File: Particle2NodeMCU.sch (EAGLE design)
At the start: 6 parts

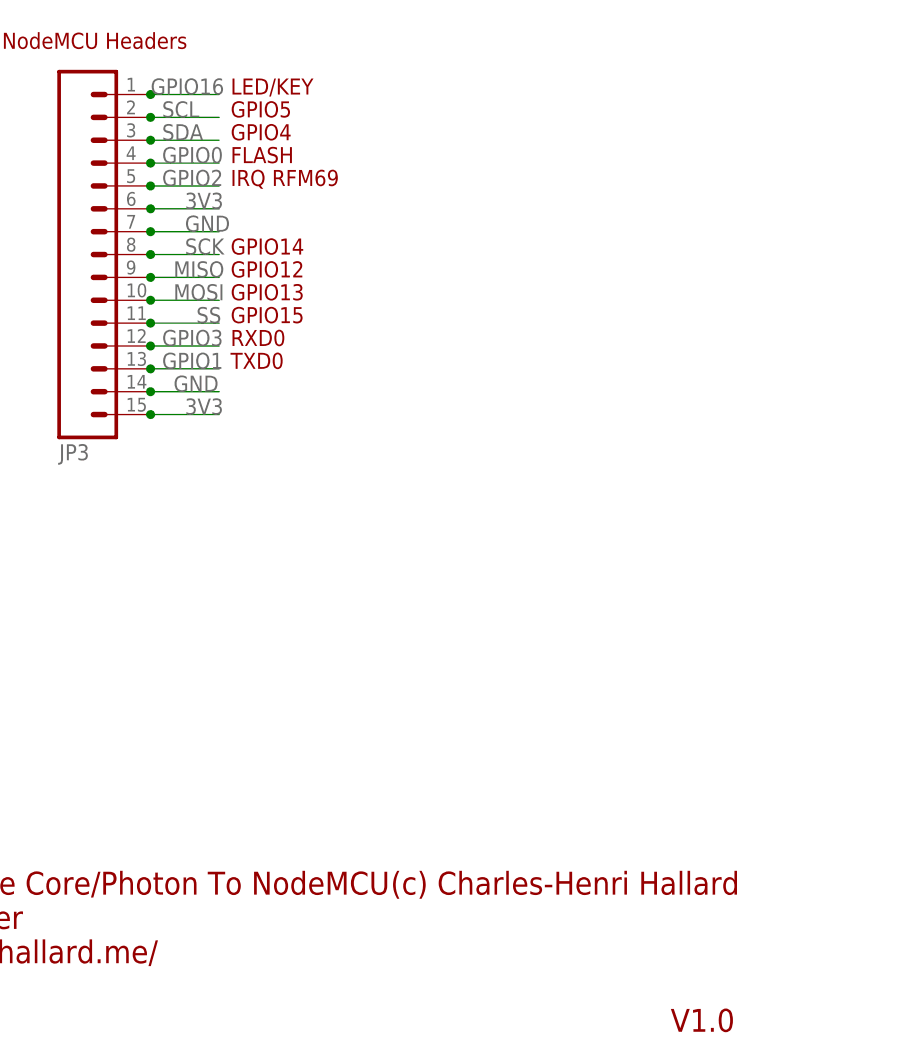
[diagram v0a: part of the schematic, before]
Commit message: Fixed GPIO now version 1.0a
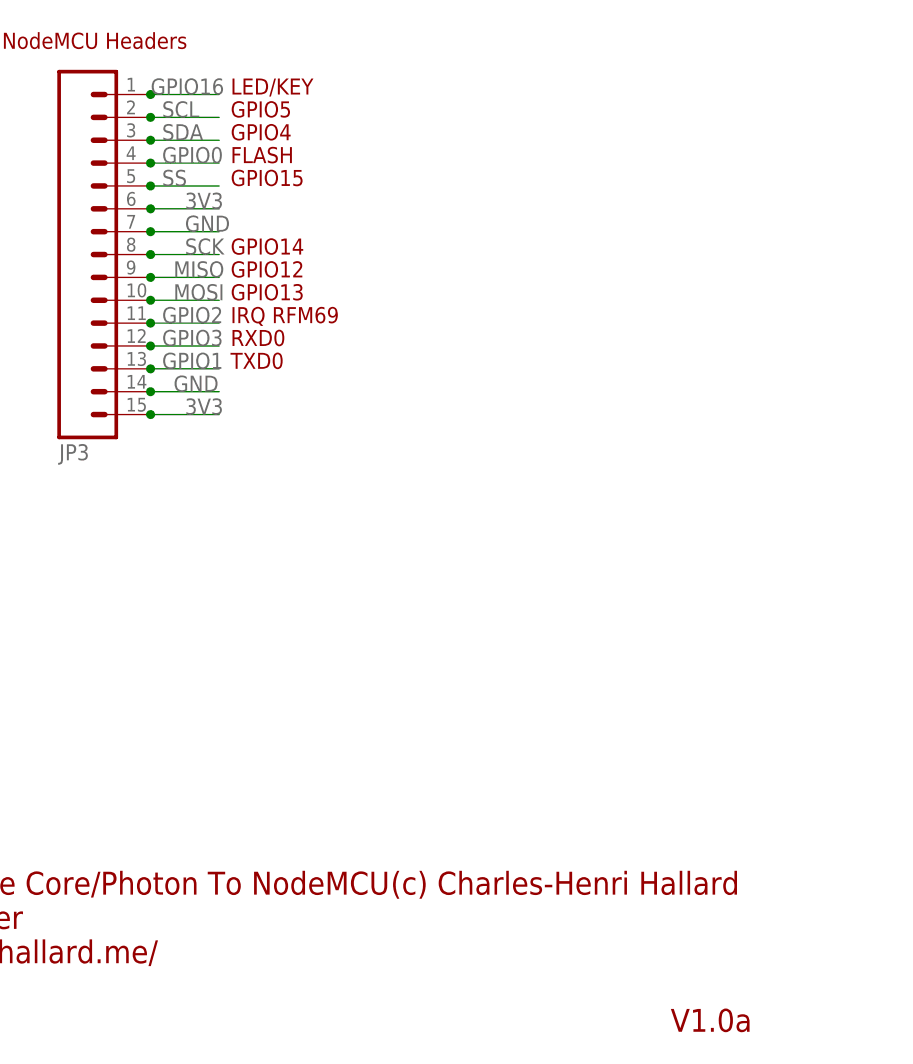
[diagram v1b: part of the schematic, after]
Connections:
- net GPIO2: now also JP3.11; no longer JP3.5
- net SS: now also JP3.5; no longer JP3.11
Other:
- note added: "V1.0a"
- note removed: "V1.0"
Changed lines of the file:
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@@
 <sheet>
 <plain>
-<text x="162.56" y="59.69" size="1.778" layer="94">IRQ RFM69</text>
+<text x="162.56" y="44.45" size="1.778" layer="94">IRQ RFM69</text>
 <text x="162.56" y="62.23" size="1.778" layer="94">FLASH</text>
 <text x="162.56" y="49.53" size="1.778" layer="94">GPIO12</text>
@@
 <text x="162.56" y="46.99" size="1.778" layer="94">GPIO13</text>
 <text x="162.56" y="52.07" size="1.778" layer="94">GPIO14</text>
-<text x="162.56" y="44.45" size="1.778" layer="94">GPIO15</text>
+<text x="162.56" y="59.69" size="1.778" layer="94">GPIO15</text>
 <text x="162.56" y="69.85" size="1.778" layer="94">LED/KEY</text>
 <text x="30.48" y="74.93" size="1.778" layer="94">NodeMCU Headers</text>
@@
 http://hallard.me/</text>
 <text x="180.34" y="-19.05" size="2.54" layer="94">(c) Charles-Henri Hallard</text>
-<text x="211.455" y="-34.29" size="2.54" layer="94">V1.0</text>
+<text x="211.455" y="-34.29" size="2.54" layer="94">V1.0a</text>
 </plain>
 <instances>
@@
 <net name="SS" class="0">
 <segment>
-<wire x1="161.29" y1="44.45" x2="153.67" y2="44.45" width="0.1524" layer="91"/>
-<label x="158.75" y="44.45" size="1.778" layer="95"/>
-<pinref part="JP3" gate="G$1" pin="11"/>
-<junction x="153.67" y="44.45"/>
-</segment>
-<segment>
 <pinref part="U$2" gate="G$1" pin="A2"/>
 <wire x1="71.12" y1="33.02" x2="60.96" y2="33.02" width="0.1524" layer="91"/>
 <label x="60.96" y="33.02" size="1.778" layer="95"/>
+</segment>
+<segment>
+<wire x1="161.29" y1="59.69" x2="153.67" y2="59.69" width="0.1524" layer="91"/>
+<label x="154.94" y="59.69" size="1.778" layer="95"/>
+<pinref part="JP3" gate="G$1" pin="5"/>
+<junction x="153.67" y="59.69"/>
 </segment>
 </net>
@@
 <net name="GPIO2" class="0">
 <segment>
-<wire x1="161.29" y1="59.69" x2="153.67" y2="59.69" width="0.1524" layer="91"/>
-<label x="154.94" y="59.69" size="1.778" layer="95"/>
-<pinref part="JP3" gate="G$1" pin="5"/>
-<junction x="153.67" y="59.69"/>
-</segment>
-<segment>
 <pinref part="U$2" gate="G$1" pin="D2"/>
 <wire x1="106.68" y1="33.02" x2="114.3" y2="33.02" width="0.1524" layer="91"/>
 <label x="109.22" y="33.02" size="1.778" layer="95"/>
 </segment>
-</net>
+<segment>
+<wire x1="161.29" y1="44.45" x2="153.67" y2="44.45" width="0.1524" layer="91"/>
+<label x="154.94" y="44.45" size="1.778" layer="95"/>
+<pinref part="JP3" gate="G$1" pin="11"/>
+<junction x="153.67" y="44.45"/>
+</segment>
+</net>

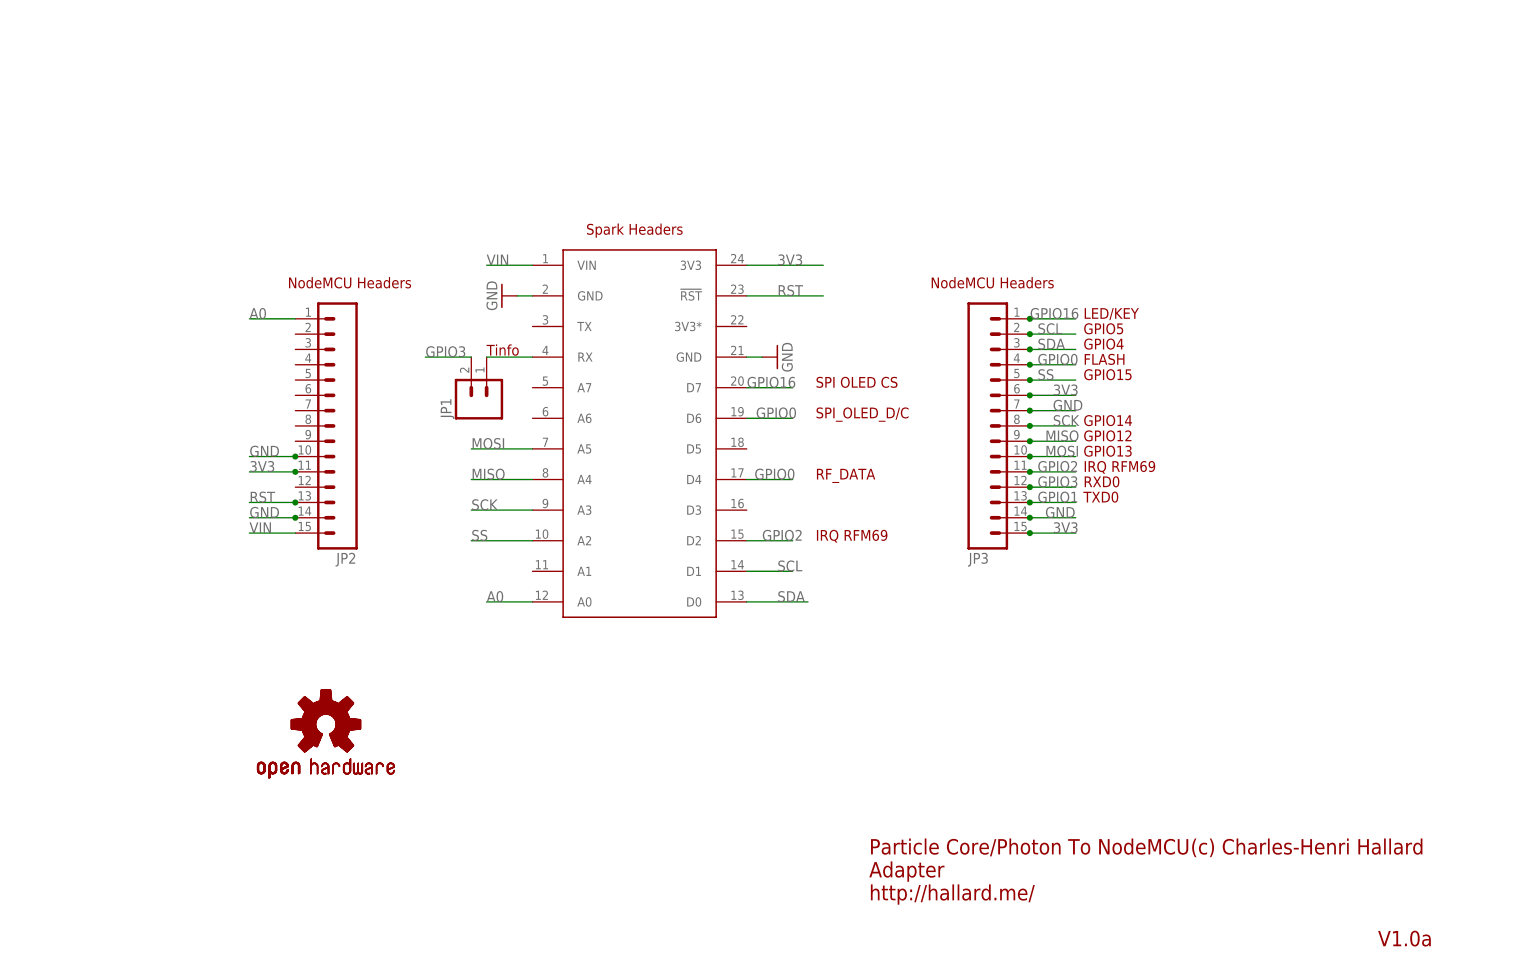
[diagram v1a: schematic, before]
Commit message: Version 1.1 ajout inverseur FET
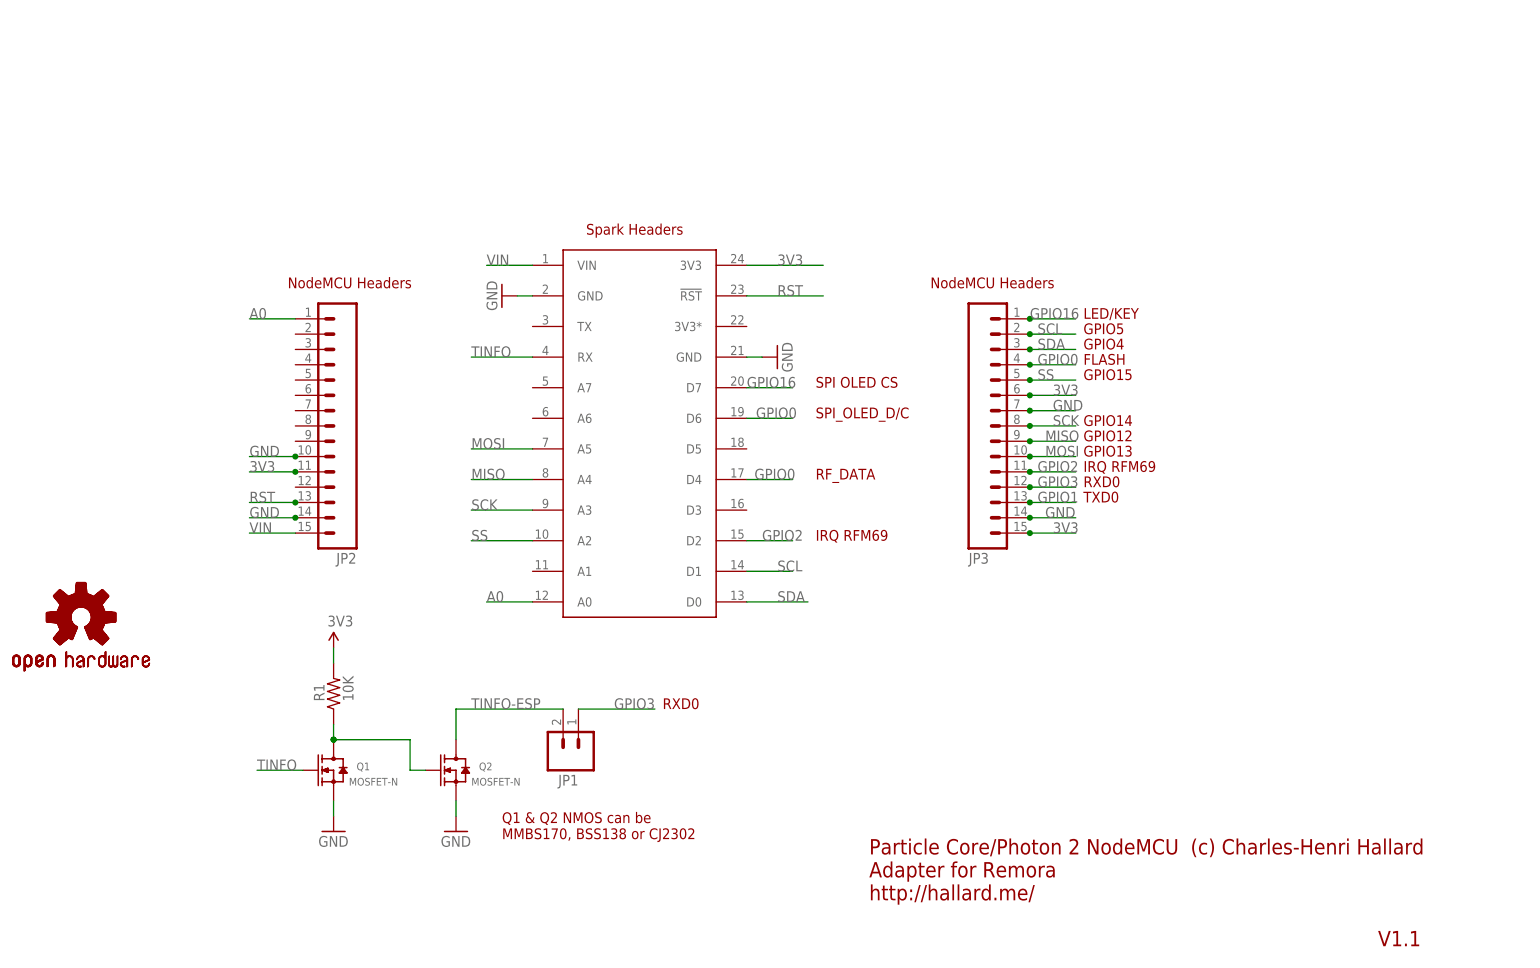
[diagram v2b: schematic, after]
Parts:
- added Q1, Q2: MOSFET-N, Seeed-Discrete:MOSFET-N-''
- added R1: 10K, _c2h:RESISTOR0805-RES
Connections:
- removed net N$1: JP1.1, U$2.RX
- new net N$3: Q1.D, Q2.G, R1.1
- new net TINFO: Q1.G, U$2.RX
- new net TINFO-ESP: JP1.2, Q2.D
- net 3V3: now also R1.2
- net GND: now also Q1.S, Q2.S
- net GPIO3: now also JP1.1; no longer JP1.2
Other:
- note added: "Particle Core/Photon 2 NodeMCU Adapter for Remora http://hallard.me/"
- note added: "Q1 & Q2 NMOS can be MMBS170, BSS138 or CJ2302"
- note added: "V1.1"
- note removed: "Particle Core/Photon To NodeMCU Adapter http://hallard.me/"
- note removed: "Tinfo"
- note removed: "V1.0a"
- moved on the sheet: JP1
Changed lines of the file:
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@@
 <part name="LOGO1" library="SparkFun-Aesthetics" deviceset="OSHW-LOGO" device="M"/>
 <part name="LOGO2" library="SparkFun-Aesthetics" deviceset="OSHW-LOGO" device="M"/>
+<part name="Q1" library="Seeed-Discrete" deviceset="MOSFET-N" device="-''" value="MOSFET-N"/>
+<part name="Q2" library="Seeed-Discrete" deviceset="MOSFET-N" device="-''" value="MOSFET-N"/>
+<part name="R1" library="_c2h" deviceset="RESISTOR" device="0805-RES" value="10K"/>
+<part name="P+1" library="_c2h" deviceset="3V3" device=""/>
+<part name="GND4" library="SparkFun" deviceset="GND" device=""/>
+<part name="GND5" library="SparkFun" deviceset="GND" device=""/>
 </parts>
 <sheets>
@@
 <text x="162.56" y="69.85" size="1.778" layer="94">LED/KEY</text>
 <text x="30.48" y="74.93" size="1.778" layer="94">NodeMCU Headers</text>
-<text x="63.5" y="63.754" size="1.778" layer="94">Tinfo</text>
 <text x="118.11" y="33.02" size="1.778" layer="94">IRQ RFM69</text>
 <text x="118.11" y="53.34" size="1.778" layer="94">SPI_OLED_D/C</text>
@@
 <text x="137.16" y="74.93" size="1.778" layer="94">NodeMCU Headers</text>
 <text x="80.01" y="83.82" size="1.778" layer="94">Spark Headers</text>
-<text x="127" y="-26.67" size="2.54" layer="94">Particle Core/Photon To NodeMCU
-Adapter
+<text x="127" y="-26.67" size="2.54" layer="94">Particle Core/Photon 2 NodeMCU
+Adapter for Remora
 http://hallard.me/</text>
 <text x="180.34" y="-19.05" size="2.54" layer="94">(c) Charles-Henri Hallard</text>
-<text x="211.455" y="-34.29" size="2.54" layer="94">V1.0a</text>
+<text x="211.455" y="-34.29" size="2.54" layer="94">V1.1</text>
+<text x="92.71" y="5.08" size="1.778" layer="94">RXD0</text>
+<text x="66.04" y="-16.51" size="1.778" layer="94">Q1 &amp; Q2 NMOS can be
+MMBS170, BSS138 or CJ2302</text>
 </plain>
 <instances>
@@
 <instance part="GND2" gate="1" x="66.04" y="73.66" rot="R270"/>
 <instance part="GND3" gate="1" x="111.76" y="63.5" rot="R90"/>
-<instance part="JP1" gate="G$1" x="63.5" y="55.88" rot="R90"/>
+<instance part="JP1" gate="G$1" x="78.74" y="-2.54" smashed="yes" rot="R90">
+<attribute name="VALUE" x="83.82" y="-5.08" size="1.778" layer="96" rot="R90"/>
+<attribute name="NAME" x="78.74" y="-5.842" size="1.778" layer="95" rot="R180"/>
+</instance>
 <instance part="JP2" gate="G$1" x="41.91" y="52.07" rot="R180"/>
 <instance part="JP3" gate="G$1" x="143.51" y="52.07" rot="MR180"/>
 <instance part="RFPIGW" gate="G$1" x="-35.56" y="-39.37"/>
-<instance part="LOGO1" gate="G$1" x="36.83" y="2.54"/>
-<instance part="LOGO2" gate="G$1" x="36.83" y="2.54"/>
+<instance part="LOGO1" gate="G$1" x="-3.81" y="20.32"/>
+<instance part="LOGO2" gate="G$1" x="-3.81" y="20.32"/>
+<instance part="Q1" gate="Q" x="38.1" y="-5.08" smashed="yes">
+<attribute name="NAME" x="41.91" y="-5.08" size="1.27" layer="95" ratio="10"/>
+<attribute name="VALUE" x="40.64" y="-7.62" size="1.27" layer="96" ratio="10"/>
+</instance>
+<instance part="Q2" gate="Q" x="58.42" y="-5.08" smashed="yes">
+<attribute name="NAME" x="62.23" y="-5.08" size="1.27" layer="95" ratio="10"/>
+<attribute name="VALUE" x="60.96" y="-7.62" size="1.27" layer="96" ratio="10"/>
+</instance>
+<instance part="R1" gate="G$1" x="38.1" y="7.62" smashed="yes" rot="R90">
+<attribute name="NAME" x="36.6014" y="6.35" size="1.778" layer="95" rot="R90"/>
+<attribute name="VALUE" x="41.402" y="6.35" size="1.778" layer="96" rot="R90"/>
+</instance>
+<instance part="P+1" gate="3V3" x="38.1" y="15.24"/>
+<instance part="GND4" gate="1" x="38.1" y="-15.24"/>
+<instance part="GND5" gate="1" x="58.42" y="-15.24"/>
 </instances>
 <busses>
@@
 <junction x="153.67" y="57.15"/>
 </segment>
+<segment>
+<pinref part="R1" gate="G$1" pin="2"/>
+<wire x1="38.1" y1="12.7" x2="38.1" y2="15.24" width="0.1524" layer="91"/>
+<pinref part="P+1" gate="3V3" pin="3V3"/>
+</segment>
 </net>
 <net name="RST" class="0">
@@
 <junction x="153.67" y="54.61"/>
 </segment>
+<segment>
+<pinref part="Q1" gate="Q" pin="S"/>
+<wire x1="38.1" y1="-12.7" x2="38.1" y2="-10.16" width="0.1524" layer="91"/>
+<pinref part="GND4" gate="1" pin="GND"/>
+</segment>
+<segment>
+<pinref part="Q2" gate="Q" pin="S"/>
+<wire x1="58.42" y1="-10.16" x2="58.42" y2="-12.7" width="0.1524" layer="91"/>
+<pinref part="GND5" gate="1" pin="GND"/>
+</segment>
 </net>
 <net name="A0" class="0">
@@
 </segment>
 </net>
-<net name="N$1" class="0">
-<segment>
-<pinref part="JP1" gate="G$1" pin="1"/>
+<net name="TINFO" class="0">
+<segment>
+<pinref part="Q1" gate="Q" pin="G"/>
+<wire x1="33.02" y1="-5.08" x2="25.4" y2="-5.08" width="0.1524" layer="91"/>
+<label x="25.4" y="-5.08" size="1.778" layer="95"/>
+</segment>
+<segment>
 <pinref part="U$2" gate="G$1" pin="RX"/>
-<wire x1="63.5" y1="63.5" x2="71.12" y2="63.5" width="0.1524" layer="91"/>
+<wire x1="71.12" y1="63.5" x2="60.96" y2="63.5" width="0.1524" layer="91"/>
+<label x="60.96" y="63.5" size="1.778" layer="95"/>
 </segment>
 </net>
@@
 </segment>
 <segment>
-<wire x1="53.34" y1="63.5" x2="60.96" y2="63.5" width="0.1524" layer="91"/>
-<label x="53.34" y="63.5" size="1.778" layer="95"/>
-<pinref part="JP1" gate="G$1" pin="2"/>
+<pinref part="JP1" gate="G$1" pin="1"/>
+<wire x1="78.74" y1="5.08" x2="91.44" y2="5.08" width="0.1524" layer="91"/>
+<label x="91.44" y="6.858" size="1.778" layer="95" rot="R180"/>
 </segment>
 </net>
@@
 </segment>
 </net>
+<net name="N$3" class="0">
+<segment>
+<pinref part="Q2" gate="Q" pin="G"/>
+<wire x1="53.34" y1="-5.08" x2="50.8" y2="-5.08" width="0.1524" layer="91"/>
+<wire x1="50.8" y1="-5.08" x2="50.8" y2="0" width="0.1524" layer="91"/>
+<wire x1="50.8" y1="0" x2="38.1" y2="0" width="0.1524" layer="91"/>
+<pinref part="Q1" gate="Q" pin="D"/>
+<pinref part="R1" gate="G$1" pin="1"/>
+<junction x="38.1" y="0"/>
+<wire x1="38.1" y1="0" x2="38.1" y2="2.54" width="0.1524" layer="91"/>
+<junction x="38.1" y="0"/>
+</segment>
+</net>
+<net name="TINFO-ESP" class="0">
+<segment>
+<pinref part="Q2" gate="Q" pin="D"/>
+<wire x1="58.42" y1="0" x2="58.42" y2="5.08" width="0.1524" layer="91"/>
+<label x="60.96" y="5.08" size="1.778" layer="95"/>
+<pinref part="JP1" gate="G$1" pin="2"/>
+<wire x1="58.42" y1="5.08" x2="76.2" y2="5.08" width="0.1524" layer="91"/>
+</segment>
+</net>

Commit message: Updated to 1.1a
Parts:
- added JP4: (no value), SparkFun-Connectors:M15
- JP2: device SparkFun-Connectors:M15 -> SparkFun-Connectors:M02LOCK
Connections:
- net GPIO2 renamed GPIO15
- net TINFO-ESP renamed TINFO-ADAPTER
- net 3V3: now also JP4.11; no longer JP2.11
- net A0: now also JP4.1; no longer JP2.1
- net GND: now also JP4.10, JP4.14; no longer JP2.10, JP2.14
- net GPIO3: now also JP2.2
- net RST: now also JP4.13; no longer JP2.13
- net TINFO: now also JP2.1
- net VIN: now also JP4.15; no longer JP2.15
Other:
- note added: "Close JP1 if Téléinfo signal is not already corrected Remora board < v1.3 Populate Q1/Q2 and R1"
- note added: "Close JP2 if Téléinfo signal is already corrected Remora board >= v1.3 Do not populate Q1/Q2 nor R1"
- note added: "From Remora board (All version)"
- note added: "Q1 & Q2 NMOS can be MMBS170, BSS138 or CJ2302 (or may be any N Mosfet)"
- note added: "V1.1a"
- note removed: "Q1 & Q2 NMOS can be MMBS170, BSS138 or CJ2302"
- note removed: "V1.1"
- moved on the sheet: JP1, JP3, Q1, Q2, R1
